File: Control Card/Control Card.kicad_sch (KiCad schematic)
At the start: 2 parts

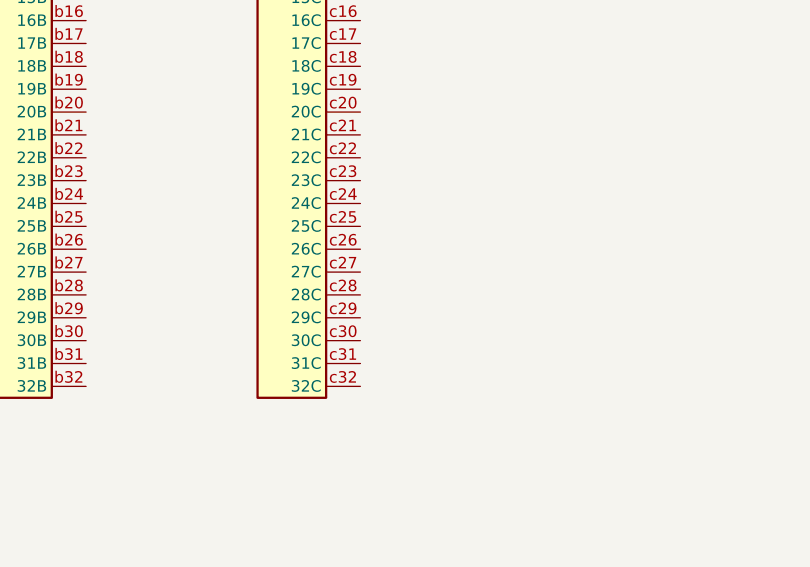
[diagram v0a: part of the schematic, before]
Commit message: add buffers for the write to the µCODE stuff
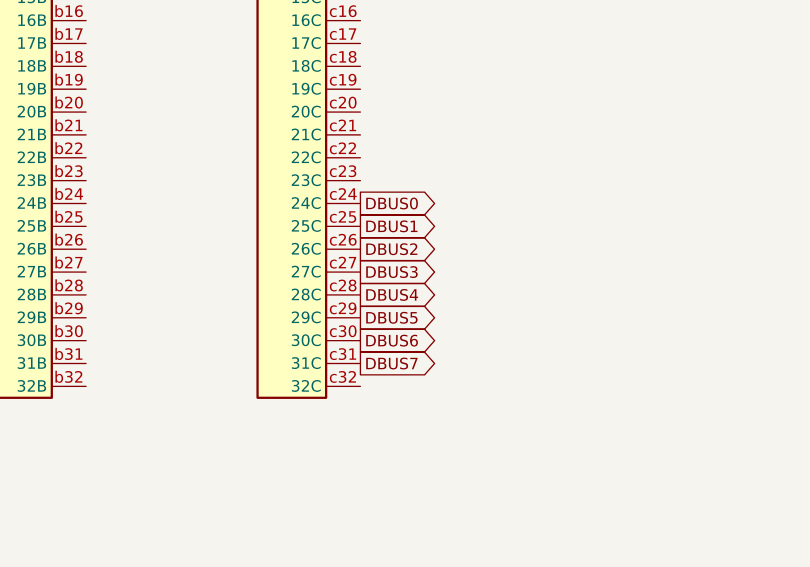
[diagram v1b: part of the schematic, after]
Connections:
- net DBUS0: now reaches J_LEFT1.c24 (24C)
- net DBUS1: now reaches J_LEFT1.c25 (25C)
- net DBUS2: now reaches J_LEFT1.c26 (26C)
- net DBUS3: now reaches J_LEFT1.c27 (27C)
- net DBUS4: now reaches J_LEFT1.c28 (28C)
- net DBUS5: now reaches J_LEFT1.c29 (29C)
- net DBUS6: now reaches J_LEFT1.c30 (30C)
- net DBUS7: now reaches J_LEFT1.c31 (31C)
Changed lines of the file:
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@@
   (page 1 2)
   (paper "A4")
+  (global_label "DBUS0" (shape output) (at 90.17 83.82 0)
+    (effects (font (size 1.27 1.27)) (justify left))
+  )
+  (global_label "DBUS1" (shape output) (at 90.17 86.36 0)
+    (effects (font (size 1.27 1.27)) (justify left))
+  )
+  (global_label "DBUS2" (shape output) (at 90.17 88.9 0)
+    (effects (font (size 1.27 1.27)) (justify left))
+  )
+  (global_label "DBUS3" (shape output) (at 90.17 91.44 0)
+    (effects (font (size 1.27 1.27)) (justify left))
+  )
+  (global_label "DBUS4" (shape output) (at 90.17 93.98 0)
+    (effects (font (size 1.27 1.27)) (justify left))
+  )
+  (global_label "DBUS5" (shape output) (at 90.17 96.52 0)
+    (effects (font (size 1.27 1.27)) (justify left))
+  )
+  (global_label "DBUS6" (shape output) (at 90.17 99.06 0)
+    (effects (font (size 1.27 1.27)) (justify left))
+  )
+  (global_label "DBUS7" (shape output) (at 90.17 101.6 0)
+    (effects (font (size 1.27 1.27)) (justify left))
+  )
   (symbol (lib_id "DIN_41612:DIN_41612_C-96") (at 22.86 64.77 0) (mirror y) (unit 1)
     (in_bom yes) (on_board yes)
@@
       (reference "#PWR0122") (unit 1) (value "GND") (footprint "")
     )
+    (path "/d2758184-b05b-4f4e-87b2-699f4f118f55/4fbd006f-959b-4484-981c-fa070589a656"
+      (reference "#PWR0123") (unit 1) (value "GND") (footprint "")
+    )
+    (path "/d2758184-b05b-4f4e-87b2-699f4f118f55/92681e96-d7cc-45d6-9bea-84ea3179163f"
+      (reference "#PWR0124") (unit 1) (value "VCC") (footprint "")
+    )
+    (path "/d2758184-b05b-4f4e-87b2-699f4f118f55/c2ce1e4a-7c77-416d-934e-0fb131724a03"
+      (reference "#PWR0125") (unit 1) (value "VCC") (footprint "")
+    )
+    (path "/d2758184-b05b-4f4e-87b2-699f4f118f55/65643932-faa1-4164-bdda-9abb68280fc2"
+      (reference "#PWR0126") (unit 1) (value "GND") (footprint "")
+    )
+    (path "/d2758184-b05b-4f4e-87b2-699f4f118f55/515ecb44-dc3f-4771-826e-524859b577c6"
+      (reference "#PWR0127") (unit 1) (value "GND") (footprint "")
+    )
+    (path "/d2758184-b05b-4f4e-87b2-699f4f118f55/90d2fdf1-e875-4d2f-9fce-be8ec18fe814"
+      (reference "#PWR0128") (unit 1) (value "GND") (footprint "")
+    )
+    (path "/d2758184-b05b-4f4e-87b2-699f4f118f55/33275b21-805d-4444-8a2a-e1a81ded6938"
+      (reference "#PWR0129") (unit 1) (value "VCC") (footprint "")
+    )
+    (path "/d2758184-b05b-4f4e-87b2-699f4f118f55/8def55b7-782e-438b-a6eb-3ebcb0aae5ed"
+      (reference "#PWR0130") (unit 1) (value "VCC") (footprint "")
+    )
+    (path "/d2758184-b05b-4f4e-87b2-699f4f118f55/35b69dcf-7c82-4b40-a9ed-d6c45ad2c183"
+      (reference "#PWR0131") (unit 1) (value "GND") (footprint "")
+    )
     (path "/d2758184-b05b-4f4e-87b2-699f4f118f55/a20c15eb-5c10-4af4-95bf-22795fe1ff62"
       (reference "U1") (unit 1) (value "CY7C1021D") (footprint "Package_SO:TSOP-II-44_10.16x18.41mm_P0.8mm")
@@
       (reference "U61") (unit 5) (value "74ACT32") (footprint "Package_SO:SOIC-14_3.9x8.7mm_P1.27mm")
     )
-    (path "/d2758184-b05b-4f4e-87b2-699f4f118f55/0ff19883-63cd-48d1-89b1-8153167ba774"
-      (reference "U100") (unit 1) (value "74LS08") (footprint "Package_SO:SOIC-14_3.9x8.7mm_P1.27mm")
-    )
-    (path "/d2758184-b05b-4f4e-87b2-699f4f118f55/1baf7460-45fa-4b23-8dde-871ce5366b84"
-      (reference "U100") (unit 2) (value "74LS08") (footprint "Package_SO:SOIC-14_3.9x8.7mm_P1.27mm")
-    )
-    (path "/d2758184-b05b-4f4e-87b2-699f4f118f55/47182dd4-c350-463c-aade-84d372f83c4f"
-      (reference "U100") (unit 3) (value "74LS08") (footprint "Package_SO:SOIC-14_3.9x8.7mm_P1.27mm")
-    )
-    (path "/d2758184-b05b-4f4e-87b2-699f4f118f55/e8ed7db2-685c-4f31-a14c-372a15bdbe3b"
-      (reference "U100") (unit 4) (value "74LS08") (footprint "Package_SO:SOIC-14_3.9x8.7mm_P1.27mm")
-    )
-    (path "/d2758184-b05b-4f4e-87b2-699f4f118f55/cb277772-7a51-4cc1-9aad-0e620e9c966a"
-      (reference "U100") (unit 5) (value "74LS08") (footprint "Package_SO:SOIC-14_3.9x8.7mm_P1.27mm")
-    )
-    (path "/d2758184-b05b-4f4e-87b2-699f4f118f55/d76b48e5-753a-4958-8543-f14fdbad3ad8"
-      (reference "U101") (unit 1) (value "74ACT32") (footprint "Package_SO:SOIC-14_3.9x8.7mm_P1.27mm")
-    )
-    (path "/d2758184-b05b-4f4e-87b2-699f4f118f55/d32ce40a-7363-499c-b257-f70896a2b364"
-      (reference "U101") (unit 2) (value "74ACT32") (footprint "Package_SO:SOIC-14_3.9x8.7mm_P1.27mm")
-    )
-    (path "/d2758184-b05b-4f4e-87b2-699f4f118f55/021e023a-4134-4222-b056-cf22d2680b61"
-      (reference "U101") (unit 3) (value "74ACT32") (footprint "Package_SO:SOIC-14_3.9x8.7mm_P1.27mm")
-    )
-    (path "/d2758184-b05b-4f4e-87b2-699f4f118f55/384327f3-e484-474c-ae1d-33771ca6364f"
-      (reference "U101") (unit 4) (value "74ACT32") (footprint "Package_SO:SOIC-14_3.9x8.7mm_P1.27mm")
-    )
-    (path "/d2758184-b05b-4f4e-87b2-699f4f118f55/0daaaf47-62ae-4afa-a2f6-8f6c1dbdf769"
-      (reference "U101") (unit 5) (value "74ACT32") (footprint "Package_SO:SOIC-14_3.9x8.7mm_P1.27mm")
-    )
-  )
+    (path "/d2758184-b05b-4f4e-87b2-699f4f118f55/d41adb8b-ee42-4416-907c-581fe1cf0750"
+      (reference "U100") (unit 1) (value "74LVC1G08") (footprint "Package_TO_SOT_SMD:SOT-23-5")
+    )
+    (path "/d2758184-b05b-4f4e-87b2-699f4f118f55/3987c192-4540-4242-90ac-9fd15e47fa66"
+      (reference "U101") (unit 1) (value "74LVC1G32") (footprint "Package_TO_SOT_SMD:SOT-23-5")
+    )
+    (path "/d2758184-b05b-4f4e-87b2-699f4f118f55/88074906-0205-4347-83ce-e778af152668"
+      (reference "U102") (unit 1) (value "74LVC1G157") (footprint "Package_SO:SSOP-8_2.95x2.8mm_P0.65mm")
+    )
+    (path "/d2758184-b05b-4f4e-87b2-699f4f118f55/a51f6340-9b6b-4dda-9ba7-852157ceaac3"
+      (reference "U110") (unit 1) (value "74ACT244") (footprint "Package_SO:SOIC-20W_7.5x12.8mm_P1.27mm")
+    )
+    (path "/d2758184-b05b-4f4e-87b2-699f4f118f55/7e41ee10-df63-44dd-8c0c-4b6e659a212b"
+      (reference "U111") (unit 1) (value "74ACT374") (footprint "Package_SO:SOIC-20W_7.5x12.8mm_P1.27mm")
+    )
+    (path "/d2758184-b05b-4f4e-87b2-699f4f118f55/8ecb5398-4850-492c-8ef6-a1fd7a8b1042"
+      (reference "U112") (unit 1) (value "74ACT374") (footprint "Package_SO:SOIC-20W_7.5x12.8mm_P1.27mm")
+    )
+    (path "/d2758184-b05b-4f4e-87b2-699f4f118f55/ed36281d-0255-47c4-ad75-0b05127bea40"
+      (reference "U113") (unit 1) (value "74ACT374") (footprint "Package_SO:SOIC-20W_7.5x12.8mm_P1.27mm")
+    )
+  )

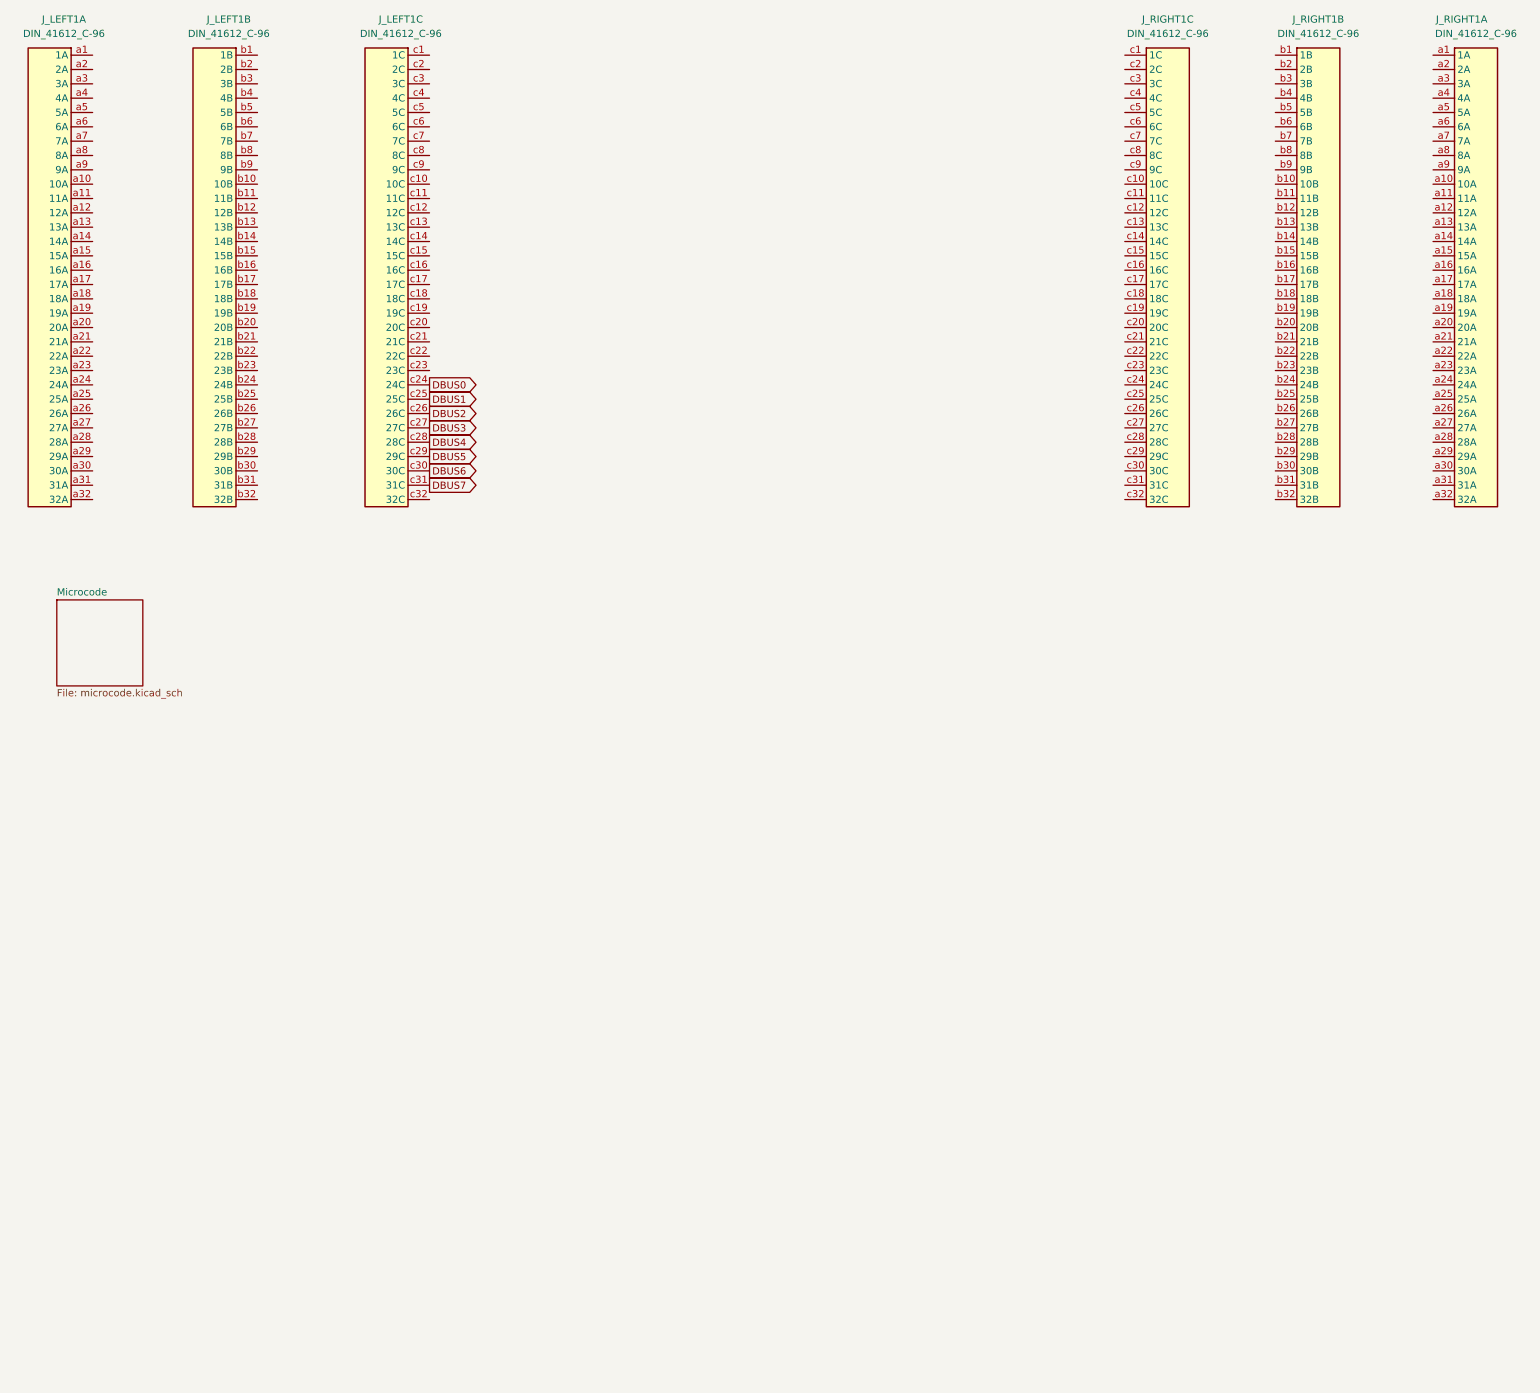
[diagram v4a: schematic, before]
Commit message: add an ESP32 as a service processor
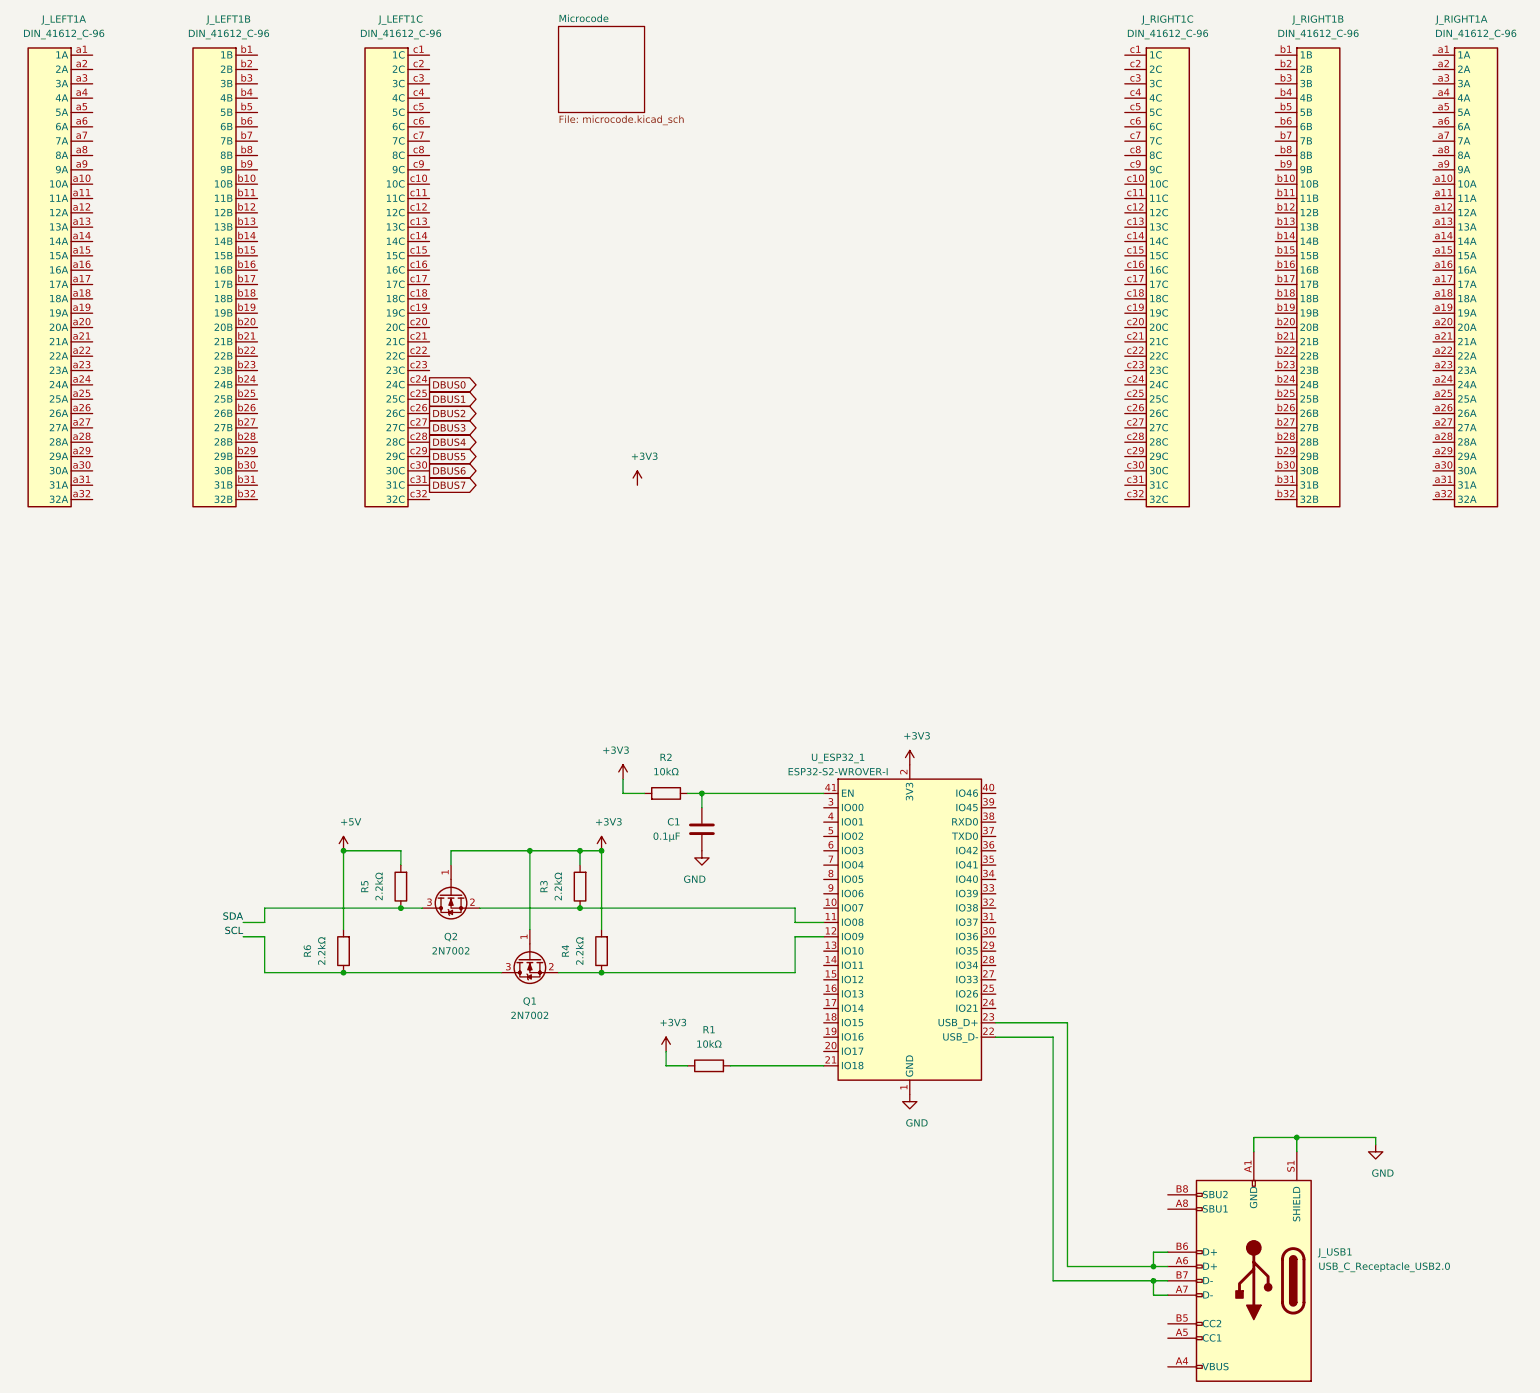
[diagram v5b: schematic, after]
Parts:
- added C1: 0.1µF, Capacitor_SMD:C_0805_2012Metric, symbol Device:C
- added J_USB1: USB_C_Receptacle_USB2.0, Connector_USB:USB_C_Receptacle_GCT_USB4085, symbol Connector:USB_C_Receptacle_USB2.0
- added Q1, Q2: 2N7002, Package_TO_SOT_SMD:SOT-23, symbol Transistor_FET:2N7002
- added R1, R2: 10kΩ, Resistor_SMD:R_0805_2012Metric, symbol Device:R
- added R3, R4, R5, R6: 2.2kΩ, Resistor_SMD:R_0805_2012Metric, symbol Device:R
- added U_ESP32_1: ESP32-S2-WROVER-I, RF_Module:ESP32-S2-WROVER, symbol RF_Module:ESP32-S2-WROVER-I
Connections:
- new net: C1.1, R2.1, U_ESP32_1.41 (EN)
- new net: Q2.2 (S), R3.1, U_ESP32_1.11 (IO08)
- new net: Q1.2 (S), R4.1, U_ESP32_1.12 (IO09)
- new net: R1.2, U_ESP32_1.21 (IO18)
- new net: J_USB1.A7 (D-), J_USB1.B7 (D-), U_ESP32_1.22 (USB_D-)
- new net: J_USB1.A6 (D+), J_USB1.B6 (D+), U_ESP32_1.23 (USB_D+)
- new net: J_USB1.A4 (VBUS), J_USB1.A9 (VBUS), J_USB1.B4 (VBUS), J_USB1.B9 (VBUS)
- new net +3V3: Q1.1 (G), Q2.1 (G), R1.1, R2.2, R3.2, R4.2, U_ESP32_1.2 (3V3)
- new net +5V: R5.2, R6.2
- new net GND: C1.2, J_USB1.A1 (GND), J_USB1.A12 (GND), J_USB1.B1 (GND), J_USB1.B12 (GND), J_USB1.S1 (SHIELD), U_ESP32_1.1 (GND), U_ESP32_1.26 (GND), U_ESP32_1.42 (GND), U_ESP32_1.43 (GND)
- new net SCL: Q1.3 (D), R6.1
- new net SDA: Q2.3 (D), R5.1
